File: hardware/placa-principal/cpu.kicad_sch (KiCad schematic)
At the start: 13 parts, among them U101 MC6809, U102 M27128A (VET 2.1), U103 HY6264LP-10, U15 74LS139, U23 74LS00

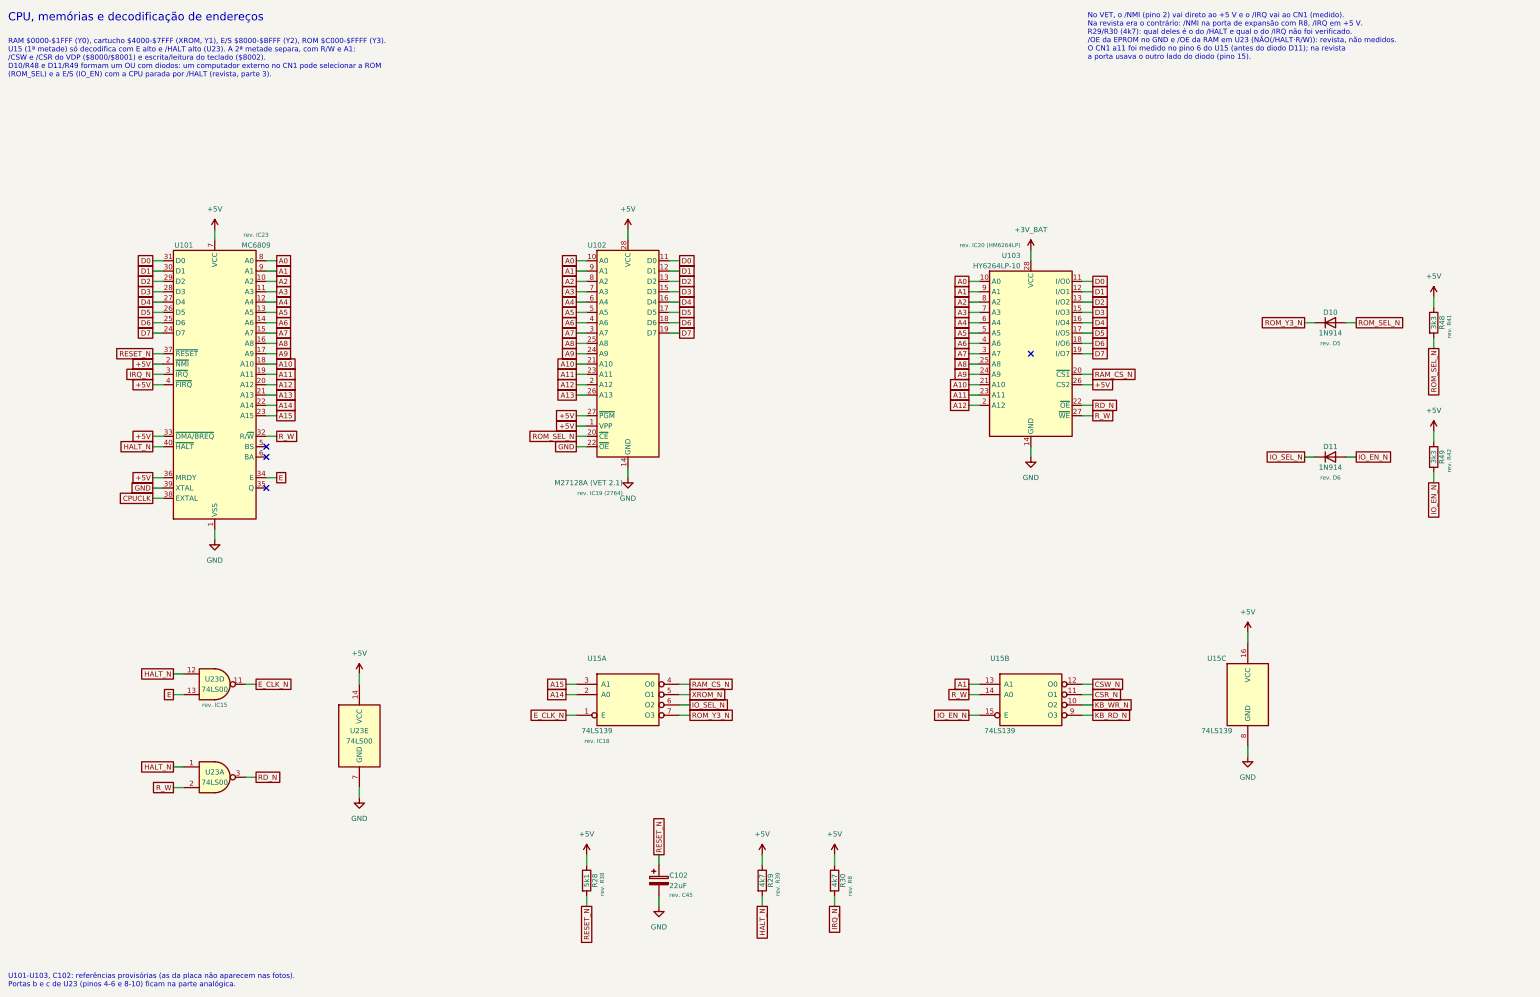
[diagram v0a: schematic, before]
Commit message: Esquema: placa da fonte e medidas do teclado, pull-ups e /OE
- Folha Fonte (fonte.kicad_sch), levantada das fotos dos dois lados da
  placa: ponte com derivação central, 7805, 7812, 7905 com bomba de carga,
  backup da RAM (+3V_BAT) e conector de saída. Explica os ~11 V no +5 V
  quando a fonte é testada sem carga.
- Teclado medido: U16 (74LS273) e U22 (74LS244) ligam D0-D7 com os mesmos
  pinos da revista (Fig. 14), e o /CLR do U16 vai ao +5 V. O conector das
  membranas é o CN3: pino 1 embaixo à esquerda, ímpares = membrana inferior
  (linhas, U16), pares = superior (colunas, U22 e R52-R59), tudo medido.
- CN2 = entrada da fonte na placa principal.
- R30 é o pull-up do /HALT e R29 o do /IRQ; /OE da EPROM e das duas
  µPD41416 no GND (medidos).
- Roteiro de continuidade: 38 redes medidas, 6 parciais, 39 só da revista.
  Docs (hardware, teclado, origem) atualizados.

Co-Authored-By: Claude Opus 5.5 <noreply@anthropic.com>
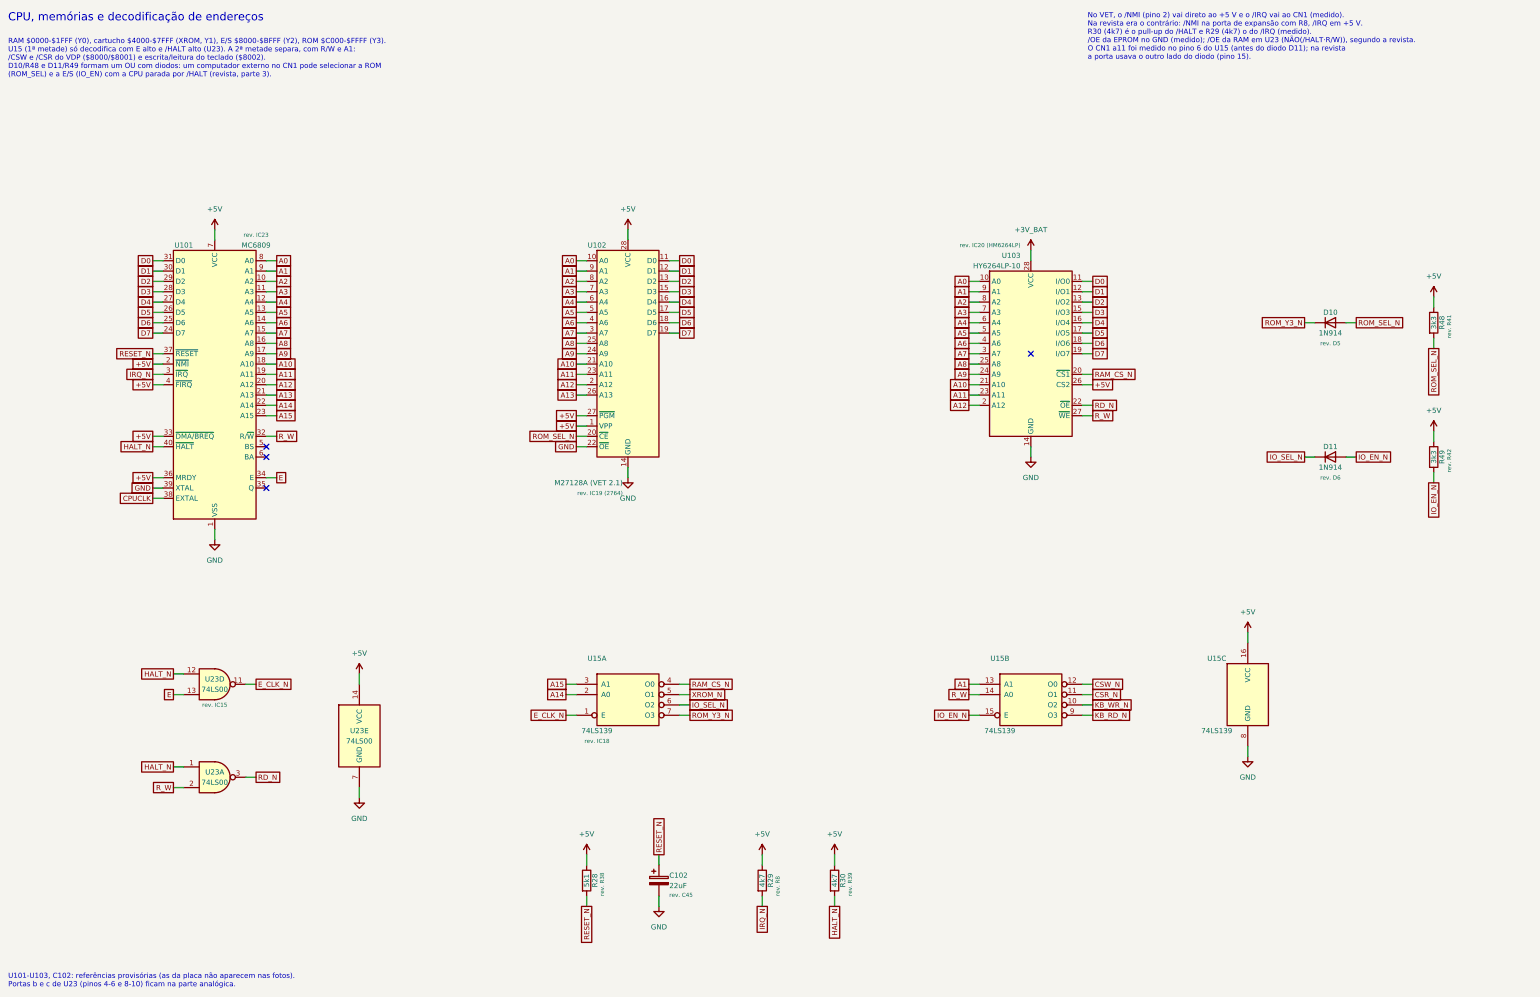
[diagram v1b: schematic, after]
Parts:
- R29: Revista rev. R39 -> rev. R8
- R30: Revista rev. R8 -> rev. R39
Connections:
- net HALT_N: now also R30.2; no longer R29.2
- net IRQ_N: now also R29.2; no longer R30.2
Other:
- note added: "No VET, o /NMI (pino 2) vai direto ao +5 V e o /IRQ vai ao CN1 (medido). Na revista era o contrário: /NMI na porta de expansão com R8, /IRQ em +5 V. R30 (4k7) é o pull-up do /HALT e R29 (4k7) o do /IRQ (medido). /OE da EPROM no GND (medido); /OE da RAM em U23 (NÃO(/HALT·R/W)), segundo a revista. O CN1 a11 foi medido no pino 6 do U15 (antes do diodo D11); na revista a porta usava o outro lado do d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"
- note removed: "No VET, o /NMI (pino 2) vai direto ao +5 V e o /IRQ vai ao CN1 (medido). Na revista era o contrário: /NMI na porta de expansão com R8, /IRQ em +5 V. R29/R30 (4k7): qual deles é o do /HALT e qual o do /IRQ não foi verificado. /OE da EPROM no GND e /OE da RAM em U23 (NÃO(/HALT·R/W)): revista, não medidos. O CN1 a11 foi medido no pino 6 do U15 (antes do diodo D11); na revista a porta usava o outro l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"
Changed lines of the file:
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@@
 		)
 	)
-	(text "No VET, o /NMI (pino 2) vai direto ao +5 V e o /IRQ vai ao CN1 (medido).\nNa revista era o contrário: /NMI na porta de expansão com R8, /IRQ em +5 V.\nR29/R30 (4k7): qual deles é o do /HALT e qual o do /IRQ não foi verificado.\n/OE da EPROM no GND e /OE da RAM em U23 (NÃO(/HALT·R/W)): revista, não medidos.\nO CN1 a11 foi medido no pino 6 do U15 (antes do diodo D11); na revista\na porta usava o outro lado do diodo (pino 15)."
+	(text "No VET, o /NMI (pino 2) vai direto ao +5 V e o /IRQ vai ao CN1 (medido).\nNa revista era o contrário: /NMI na porta de expansão com R8, /IRQ em +5 V.\nR30 (4k7) é o pull-up do /HALT e R29 (4k7) o do /IRQ (medido).\n/OE da EPROM no GND (medido); /OE da RAM em U23 (NÃO(/HALT·R/W)), segundo a revista.\nO CN1 a11 foi medido no pino 6 do U15 (antes do diodo D11); na revista\na porta usava o outro lado do diodo (pino 15)."
 		(exclude_from_sim no)
 		(at 290.83 20.32 0)
@@
 		)
 	)
-	(global_label "HALT_N"
+	(global_label "IRQ_N"
 		(shape passive)
 		(at 210.82 240.03 270)
@@
 		)
 	)
-	(global_label "IRQ_N"
+	(global_label "HALT_N"
 		(shape passive)
 		(at 228.6 240.03 270)
@@
 			)
 		)
-		(property "Revista" "rev. R39"
+		(property "Revista" "rev. R8"
 			(at 214.63 237.49 90)
 			(show_name no)
@@
 			)
 		)
-		(property "Revista" "rev. R8"
+		(property "Revista" "rev. R39"
 			(at 232.41 237.49 90)
 			(show_name no)
